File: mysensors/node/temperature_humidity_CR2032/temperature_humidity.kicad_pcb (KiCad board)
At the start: 2 copper layers, 35.9 x 35.9 mm, 33 parts, among them CON1 AVR-ISP-6, IC1 ATMEGA328P, P1 ANTENNA, U1 AT25DF512C, U2 ATSHA204A, U3 Si7021, U4 RFM69W, U5 NCP1402

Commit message: [mysensors nodes] cleaned up projects a little bit
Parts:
- U2: value ATSHA204A -> ATSHA204
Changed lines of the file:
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@@
-(kicad_pcb (version 20160815) (host pcbnew no-vcs-found-7500~57~ubuntu16.04.1)
+(kicad_pcb (version 20160815) (host pcbnew no-vcs-found-7518~57~ubuntu16.04.1)
   (general
     (links 83)
@@
     (pad 1 smd rect (at -2.5 2 180) (size 1.27 2.5) (layers F.Cu F.Paste F.Mask)
       (net 5 /MISO))
-    (model Pin_Headers.3dshapes/Pin_Header_Straight_SMT_02x03.wrl
-      (at (xyz 0 0 0))
-      (scale (xyz 1 1 1))
-      (rotate (xyz 0 0 0))
-    )
   )
   (module Symbols:OSHW-Logo_5.7x6mm_SilkScreen (layer B.Cu)
@@
       (effects (font (size 0.6 0.6) (thickness 0.12)))
     )
-    (fp_text value ATSHA204A (at -0.206 3.552) (layer F.SilkS)
-      (effects (font (size 0.6 0.6) (thickness 0.12)))
-    )
+    (fp_text value ATSHA204 (at -0.406 3.552) (layer F.SilkS)
+      (effects (font (size 0.6 0.6) (thickness 0.12)))
+    )

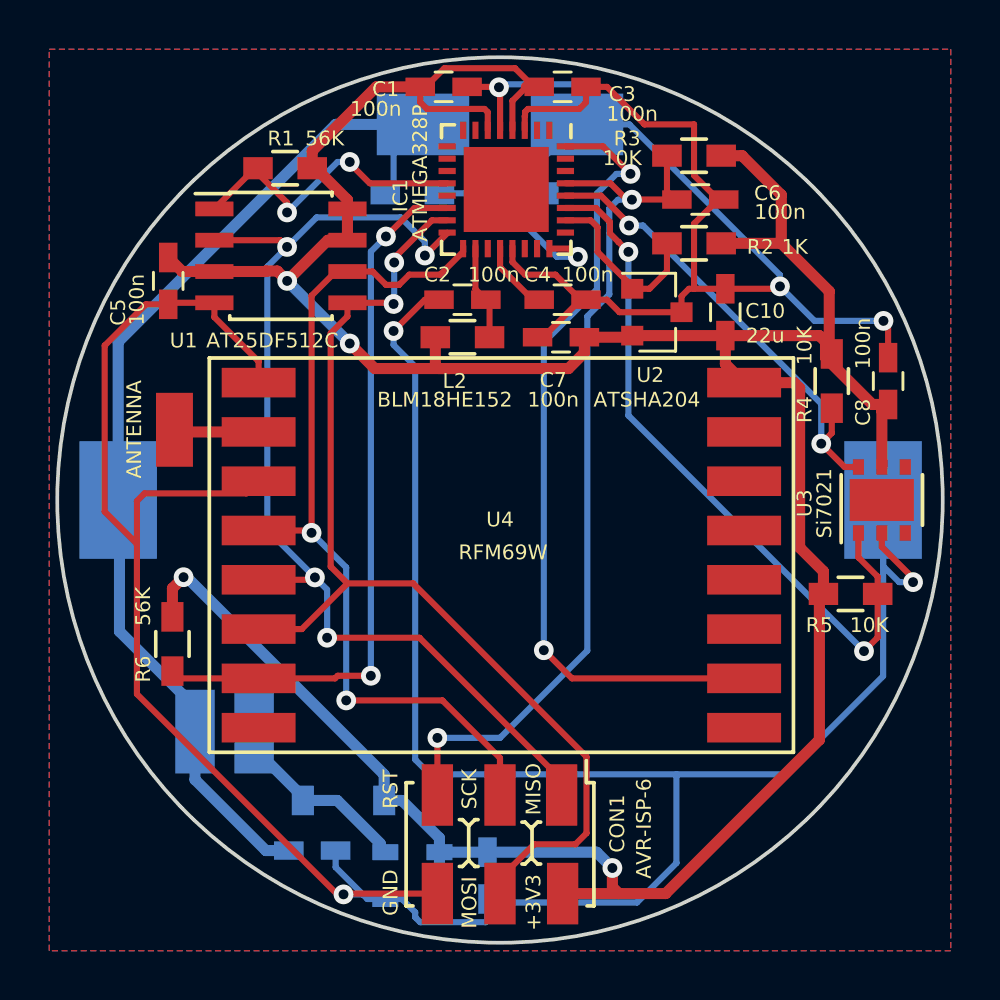
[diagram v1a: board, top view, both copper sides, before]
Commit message: [mysensors temperature_humidity_CR2032] added step-up converter bypass jumpers
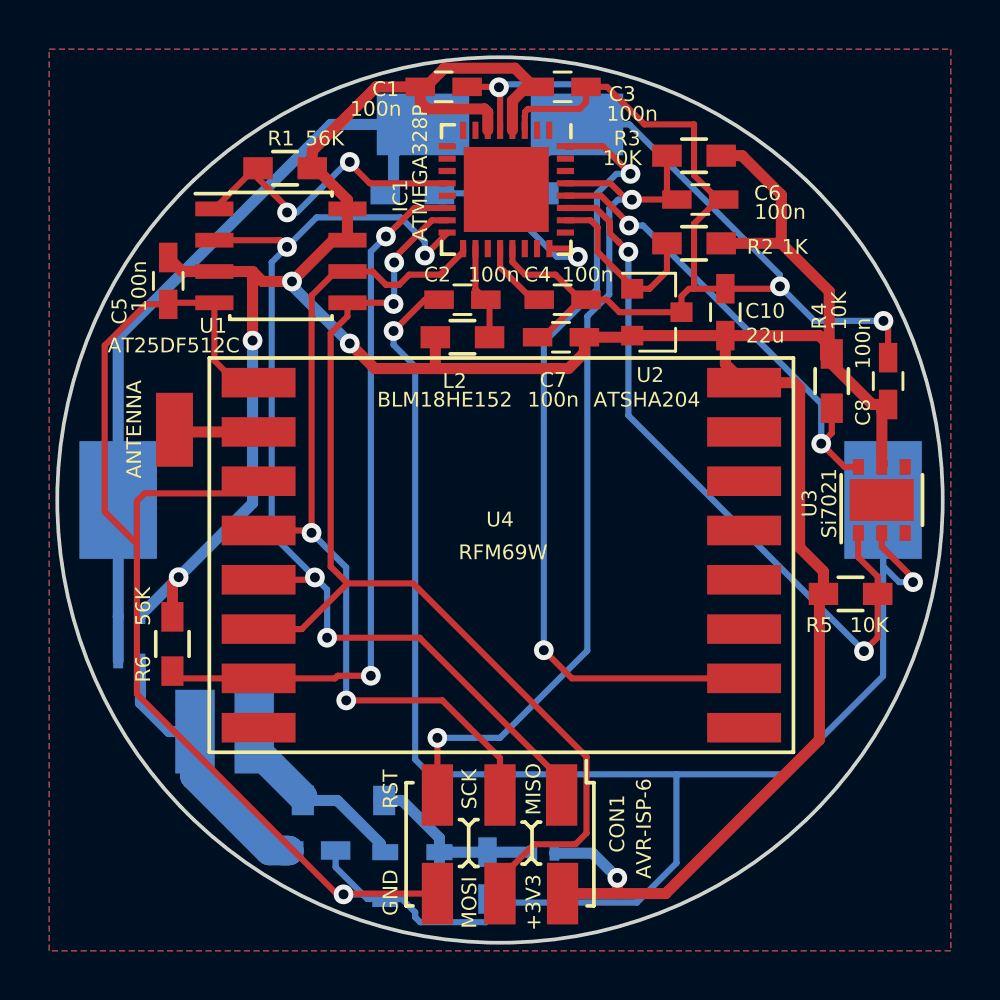
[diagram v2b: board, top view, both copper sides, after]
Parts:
- added JP1: VB_EN, Resistors_SMD:R_0402, B.Cu at (101.8, 93.4)
- added JP2: VB_DIS, Resistors_SMD:R_0402, B.Cu at (101.8, 91.6)
- added JP3: VB_EN, Resistors_SMD:R_0402, B.Cu at (118.6, 101.2)
- moved REF*** 0.57 mm to (127.2, 97.2)
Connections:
- BT1 pad 1: /V_BATT -> Net-(BT1-Pad1)
- C11 pad 1: /V_BATT -> Net-(BT1-Pad1)
- C12 pad 2: +3V3 -> Net-(C12-Pad2)
- C9 pad 2: /V_BATT -> /VB_IN
- D1 pad 1: +3V3 -> Net-(C12-Pad2)
- L1 pad 1: /V_BATT -> /VB_IN
- R7 pad 2: /V_BATT -> Net-(BT1-Pad1)
- U5 pad 1: +3V3 -> Net-(C12-Pad2)
- U5 pad 2: +3V3 -> Net-(C12-Pad2)
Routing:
- net /V_BATT: track 44.0 -> 0.00 mm
- net Net-(BT1-Pad1): track 0.00 -> 32.9 mm
- net /VB_IN: track 0.00 -> 11.5 mm
- net Net-(C12-Pad2): track 0.00 -> 8.51 mm
- net +3V3: track 135.6 -> 129.8 mm, vias 4 -> 5
- net GND: track 186.1 -> 186.6 mm
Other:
- board text added: "Rev. 0.2"
- board text removed: "Rev. 0.1"
